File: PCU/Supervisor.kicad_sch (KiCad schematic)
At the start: 45 parts, among them IC36 TCAN3403DDFRQ1, IC38 STM32G473CCT3, J19 JST SH 5Pin, J20 JST SH 3Pin, J21 USB4120-03-C, Y5 ECS-80-10-30B-CWN-TR

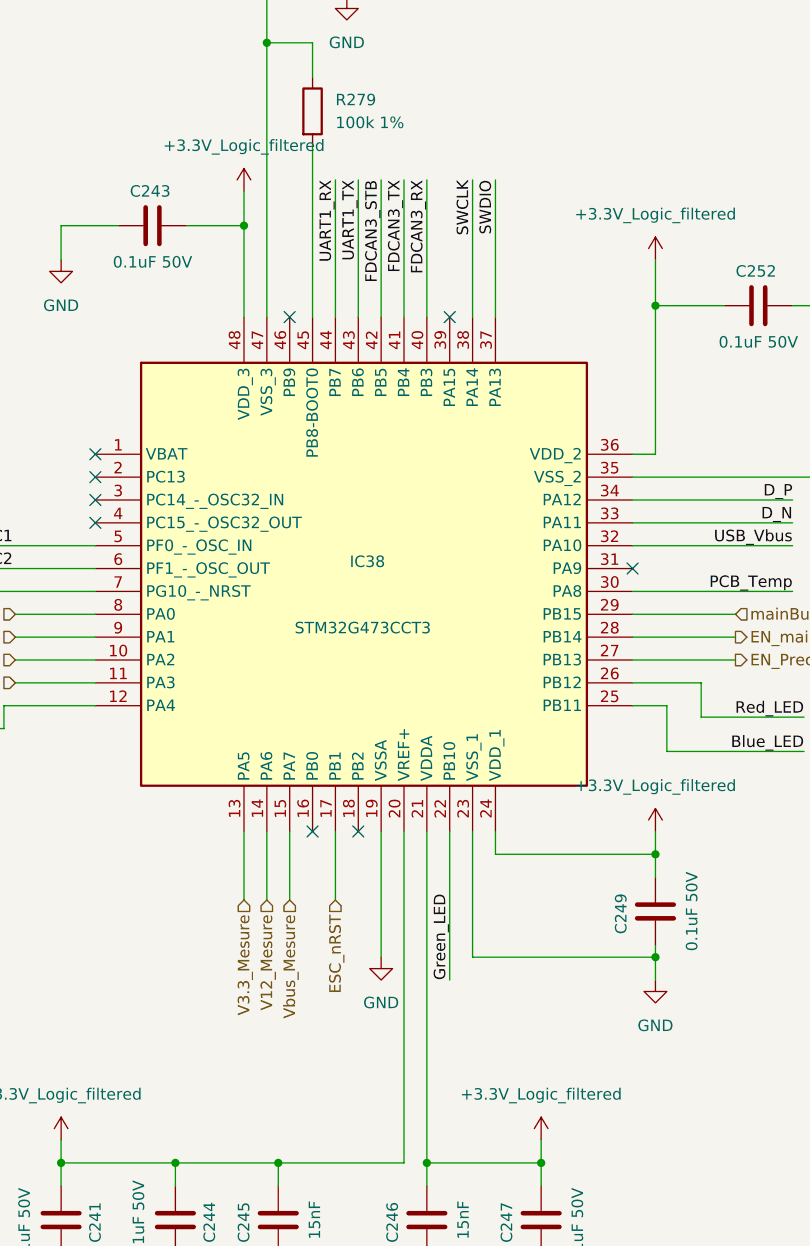
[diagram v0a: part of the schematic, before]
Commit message: Digital signals routed
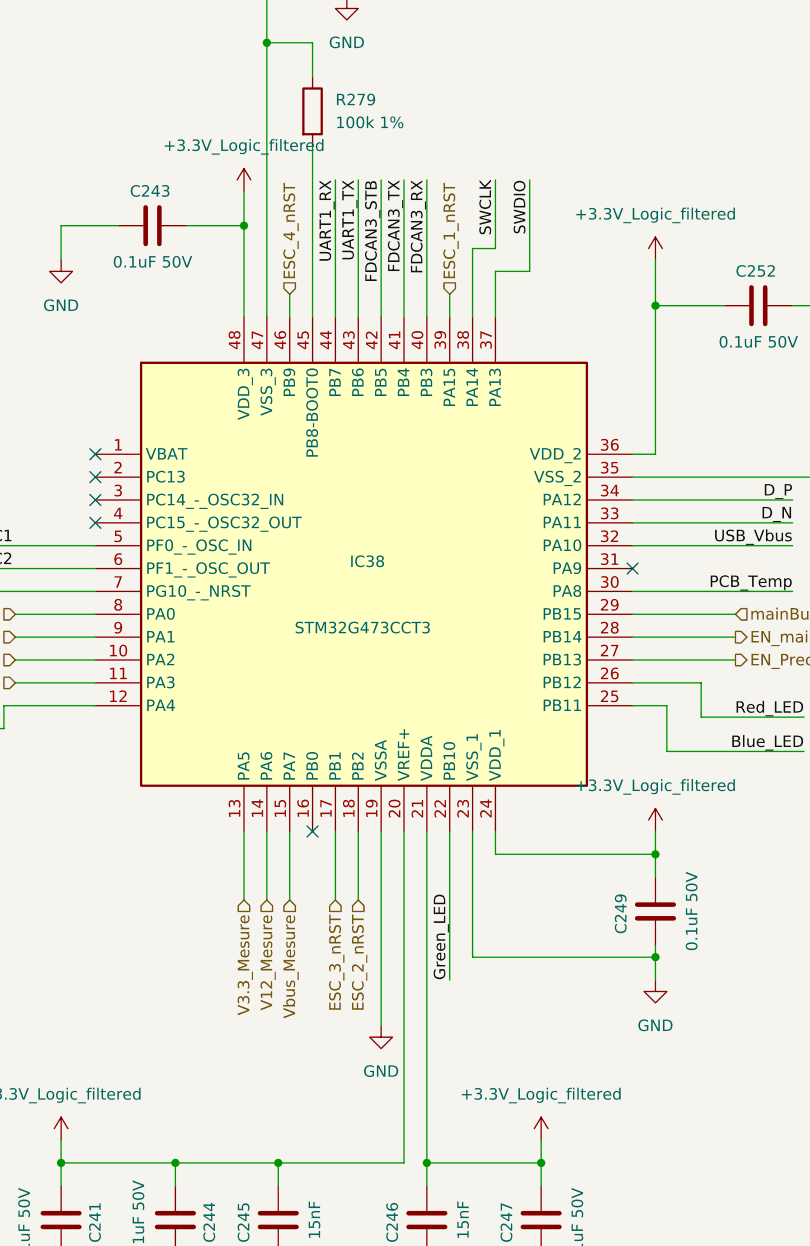
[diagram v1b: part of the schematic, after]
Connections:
- net ESC_2_nRST: now reaches IC38.18 (PB2)
- net ESC_1_nRST: now reaches IC38.39 (PA15)
- net ESC_4_nRST: now reaches IC38.46 (PB9)
- net ESC_nRST renamed ESC_3_nRST
- no-connect marks 11 -> 8
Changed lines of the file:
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@@
-	)
-	(no_connect
-		(at 158.75 152.4)
 	)
 	(no_connect
@@
 	)
 	(no_connect
-		(at 140.97 152.4)
-	)
-	(no_connect
 		(at 119.38 172.72)
 	)
@@
 	)
 	(no_connect
-		(at 148.59 209.55)
-	)
-	(no_connect
 		(at 179.07 180.34)
 	)
@@
 	(wire
 		(pts
+			(xy 163.83 137.16) (xy 163.83 144.78)
+		)
+		(stroke
+			(width 0)
+			(type default)
+		)
+	)
+	(wire
+		(pts
 			(xy 48.26 218.44) (xy 55.88 218.44)
 		)
@@
 	(wire
 		(pts
+			(xy 158.75 149.86) (xy 158.75 152.4)
+		)
+		(stroke
+			(width 0)
+			(type default)
+		)
+	)
+	(wire
+		(pts
 			(xy 68.58 245.11) (xy 55.88 245.11)
 		)
@@
 	(wire
 		(pts
+			(xy 148.59 209.55) (xy 148.59 217.17)
+		)
+		(stroke
+			(width 0)
+			(type default)
+		)
+	)
+	(wire
+		(pts
 			(xy 156.21 137.16) (xy 156.21 152.4)
 		)
@@
 	(wire
 		(pts
+			(xy 140.97 149.86) (xy 140.97 152.4)
+		)
+		(stroke
+			(width 0)
+			(type default)
+		)
+	)
+	(wire
+		(pts
 			(xy 146.05 137.16) (xy 146.05 152.4)
 		)
@@
 	(wire
 		(pts
-			(xy 163.83 137.16) (xy 163.83 152.4)
+			(xy 167.64 137.16) (xy 167.64 147.32)
 		)
 		(stroke
@@
 	(wire
 		(pts
+			(xy 161.29 144.78) (xy 161.29 152.4)
+		)
+		(stroke
+			(width 0)
+			(type default)
+		)
+	)
+	(wire
+		(pts
 			(xy 168.91 59.69) (xy 168.91 57.15)
 		)
@@
 	(wire
 		(pts
+			(xy 163.83 144.78) (xy 161.29 144.78)
+		)
+		(stroke
+			(width 0)
+			(type default)
+		)
+	)
+	(wire
+		(pts
 			(xy 153.67 137.16) (xy 153.67 152.4)
 		)
@@
 	(wire
 		(pts
-			(xy 151.13 209.55) (xy 151.13 223.52)
+			(xy 151.13 209.55) (xy 151.13 231.14)
 		)
 		(stroke
@@
 	(wire
 		(pts
+			(xy 167.64 147.32) (xy 163.83 147.32)
+		)
+		(stroke
+			(width 0)
+			(type default)
+		)
+	)
+	(wire
+		(pts
 			(xy 168.91 57.15) (xy 156.21 57.15)
 		)
@@
 	(wire
 		(pts
-			(xy 161.29 137.16) (xy 161.29 152.4)
+			(xy 163.83 147.32) (xy 163.83 152.4)
 		)
 		(stroke
@@
 	)
 	(label "SWCLK"
-		(at 161.29 137.16 270)
+		(at 163.83 137.16 270)
 		(effects
 			(font
@@
 	)
 	(label "SWDIO"
-		(at 163.83 137.16 270)
+		(at 167.64 137.16 270)
 		(effects
 			(font
@@
 		)
 	)
+	(hierarchical_label "ESC_4_nRST"
+		(shape input)
+		(at 140.97 149.86 90)
+		(effects
+			(font
+				(size 1.27 1.27)
+			)
+			(justify left)
+		)
+	)
 	(hierarchical_label "EN_mainBus"
 		(shape output)
@@
 		)
 	)
+	(hierarchical_label "ESC_1_nRST"
+		(shape input)
+		(at 158.75 149.86 90)
+		(effects
+			(font
+				(size 1.27 1.27)
+			)
+			(justify left)
+		)
+	)
 	(hierarchical_label "V3.3_Mesure"
 		(shape input)
@@
 		)
 	)
-	(hierarchical_label "ESC_nRST"
+	(hierarchical_label "ESC_3_nRST"
 		(shape input)
 		(at 146.05 217.17 270)
+		(effects
+			(font
+				(size 1.27 1.27)
+			)
+			(justify right)
+		)
+	)
+	(hierarchical_label "ESC_2_nRST"
+		(shape input)
+		(at 148.59 217.17 270)
 		(effects
 			(font
@@
 	(symbol
 		(lib_id "power:GND")
-		(at 151.13 223.52 0)
+		(at 151.13 231.14 0)
 		(unit 1)
 		(exclude_from_sim no)
@@
 		(fields_autoplaced yes)
 		(property "Reference" "#PWR0465"
-			(at 151.13 229.87 0)
+			(at 151.13 237.49 0)
 			(effects
 				(font
@@
 		)
 		(property "Value" "GND"
-			(at 151.13 228.6 0)
+			(at 151.13 236.22 0)
 			(effects
 				(font
@@
 		)
 		(property "Footprint" ""
-			(at 151.13 223.52 0)
+			(at 151.13 231.14 0)
 			(effects
 				(font
@@
 		)
 		(property "Datasheet" ""
-			(at 151.13 223.52 0)
+			(at 151.13 231.14 0)
 			(effects
 				(font
@@
 		)
 		(property "Description" "Power symbol creates a global label with name \"GND\" , ground"
-			(at 151.13 223.52 0)
+			(at 151.13 231.14 0)
 			(effects
 				(font

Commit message: Components library added
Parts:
- J19, J20: now in the parts list
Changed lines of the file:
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@@
 		(unit 1)
 		(exclude_from_sim no)
-		(in_bom no)
+		(in_bom yes)
 		(on_board yes)
 		(dnp no)
@@
 		(unit 1)
 		(exclude_from_sim no)
-		(in_bom no)
+		(in_bom yes)
 		(on_board yes)
 		(dnp no)
@@
 	)
 	(symbol
+		(lib_name "Thermistor_NTC_1")
 		(lib_id "Device:Thermistor_NTC")
 		(at 356.87 205.74 0)
@@
 			)
 		)
-		(property "Datasheet" "~"
+		(property "Datasheet" "https://www.mouser.fr/datasheet/2/281/NCU18XH103D60RB-1519634.pdf"
 			(at 356.87 204.47 0)
 			(effects

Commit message: Fly controller design started
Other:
- company: BASSINGA Lab -> BASSINGA_LAB
- title: (none) -> Propulsion Control Unit
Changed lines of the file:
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@@
 	(paper "A3")
 	(title_block
+		(title "Propulsion Control Unit")
 		(date "2025-05-21")
 		(rev "v1.0")
-		(company "BASSINGA Lab")
+		(company "BASSINGA_LAB")
+		(comment 1 "Copyright © 2025 Andresse Brisel BASSINGA ")
 	)
 	(rectangle
